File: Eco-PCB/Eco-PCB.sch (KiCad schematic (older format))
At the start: 14 parts, among them J1 DB25_Female, M1 SD Card, M1_1 XSOURCE Wireless, P1 Power_Block

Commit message: Removed unnecessary files and only kept the updated ones
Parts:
- Arduino2, Arduino3, Master1: footprint Module:Arduino_Nano_WithMountingHoles -> Module:Arduino_Nano; symbol arduino_nano:Arduino_Nano -> Eco-PCB-rescue:Arduino_Nano-arduino_nano
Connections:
- net labels added: RX_, SET, TX_
- wire segments 178 -> 202
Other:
- note added: "DT and SW for encoder from \nD14 & D15 to DSUB pins 8 & 7 respectively"

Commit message: Pcb 1 design done V1.0
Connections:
- net GND: now also J1.25 (P25); no longer J1.12
- net VCC: now also J1.13; no longer J1.25 (P25)
- net VCC_1: now also J1.23 (P23); no longer J1.13
- net at Master1.19 (AD0/D14): now also Arduino3.2 (D0/TX); no longer Arduino3.1 (D1/RX)
- net at Master1.20 (AD1/D15): now also Arduino3.1 (D1/RX); no longer Arduino3.2 (D0/TX)
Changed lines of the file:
@@
 	6050 1700 5800 1700
-Wire Wire Line
-	6350 3800 6350 3200
-Wire Wire Line
-	6350 3200 5800 3200
-Wire Wire Line
-	6450 3700 6450 3100
-Wire Wire Line
-	6450 3100 5800 3100
 Wire Wire Line
 	3900 4400 3900 3650
@@
 	6450 3700 7100 3700
 Wire Wire Line
-	8450 1750 10700 1750
-Connection ~ 10700 1750
-Wire Wire Line
 	10700 1750 10700 3400
 Wire Wire Line
@@
 NoConn ~ 9250 4550
 Wire Wire Line
-	10700 1000 10700 1750
-Wire Wire Line
 	8450 3400 8800 3400
 Wire Wire Line
@@
 	8800 2750 10800 2750
 Wire Wire Line
-	10800 2750 10800 1000
-Wire Wire Line
 	10800 4950 10800 4600
 Wire Wire Line
 	7450 4950 10800 4950
-Connection ~ 10800 2750
 Wire Wire Line
 	5150 5800 10800 5800
@@
 	10800 5900 10900 5900
 Wire Wire Line
-	10900 5900 10900 1000
+	10900 5900 10900 1200
 Text Label 10700 6200 0    50   ~ 0
 GND
@@
 Wire Wire Line
 	5150 6550 5850 6550
+Connection ~ 10800 2750
+Wire Wire Line
+	10800 2750 10800 1100
+Wire Wire Line
+	10800 1100 10900 1100
+Wire Wire Line
+	10900 1100 10900 1000
+Wire Wire Line
+	10400 1200 10400 1000
+Wire Wire Line
+	10400 1200 10900 1200
+Wire Wire Line
+	10800 1000 10750 1000
+Wire Wire Line
+	10750 1000 10750 1750
+Connection ~ 10700 1750
+Wire Wire Line
+	10700 1750 10750 1750
+Wire Wire Line
+	8450 1750 10700 1750
+Wire Wire Line
+	6350 3100 5800 3100
+Wire Wire Line
+	6350 3100 6350 3800
+Wire Wire Line
+	6450 3050 5900 3050
+Wire Wire Line
+	5900 3050 5900 3200
+Wire Wire Line
+	5900 3200 5800 3200
+Wire Wire Line
+	6450 3050 6450 3700
 $EndSCHEMATC

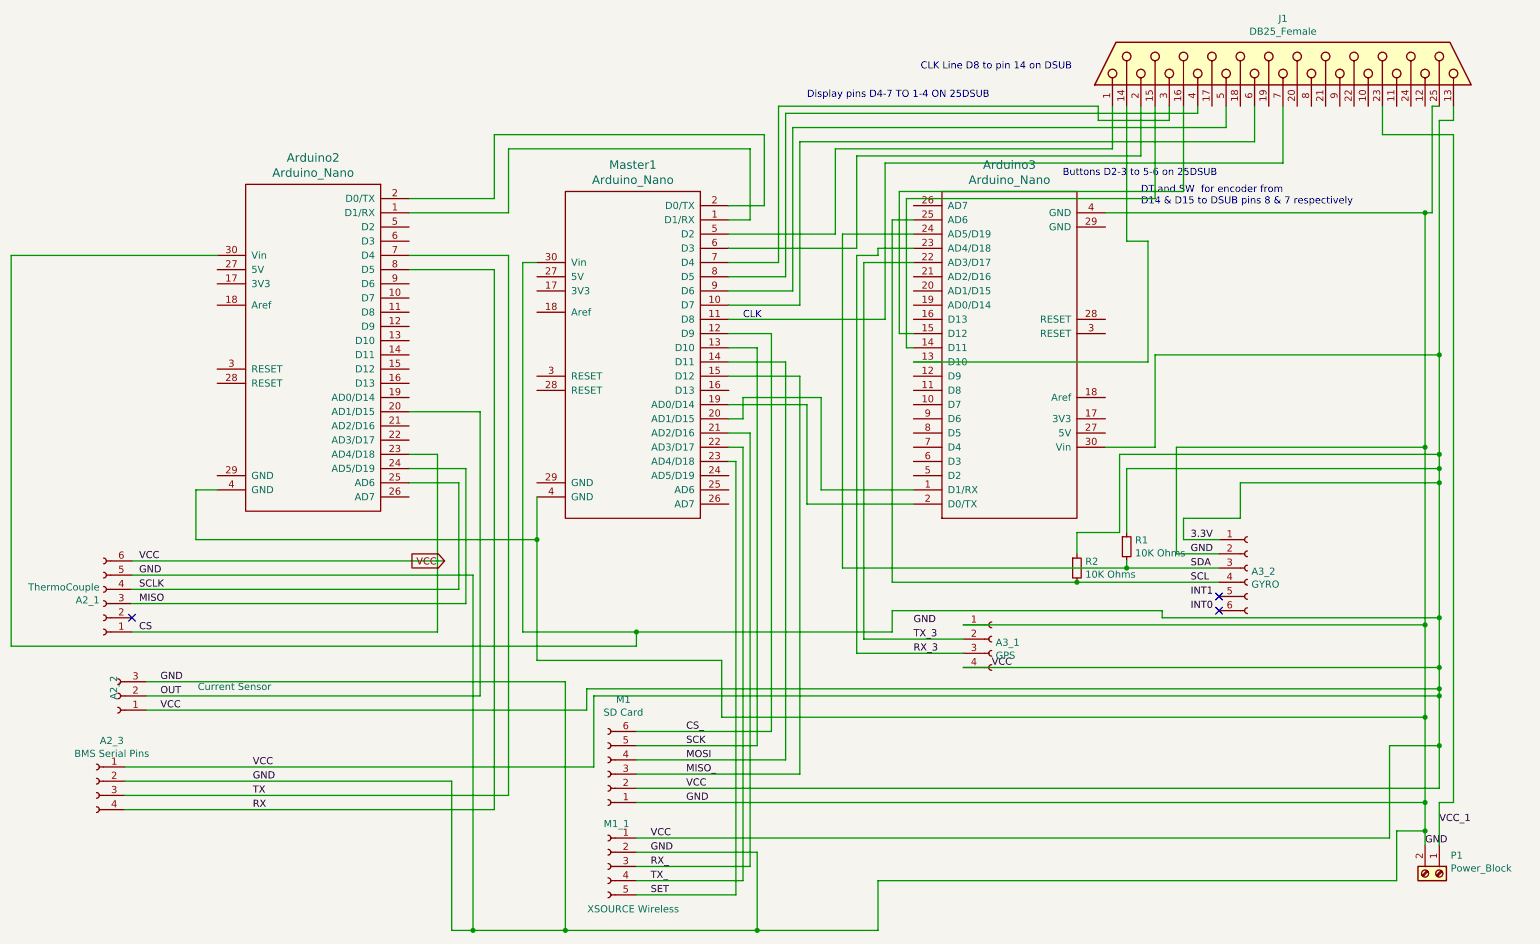
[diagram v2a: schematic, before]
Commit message: PCB1 added CLK line & PCB2 Design done
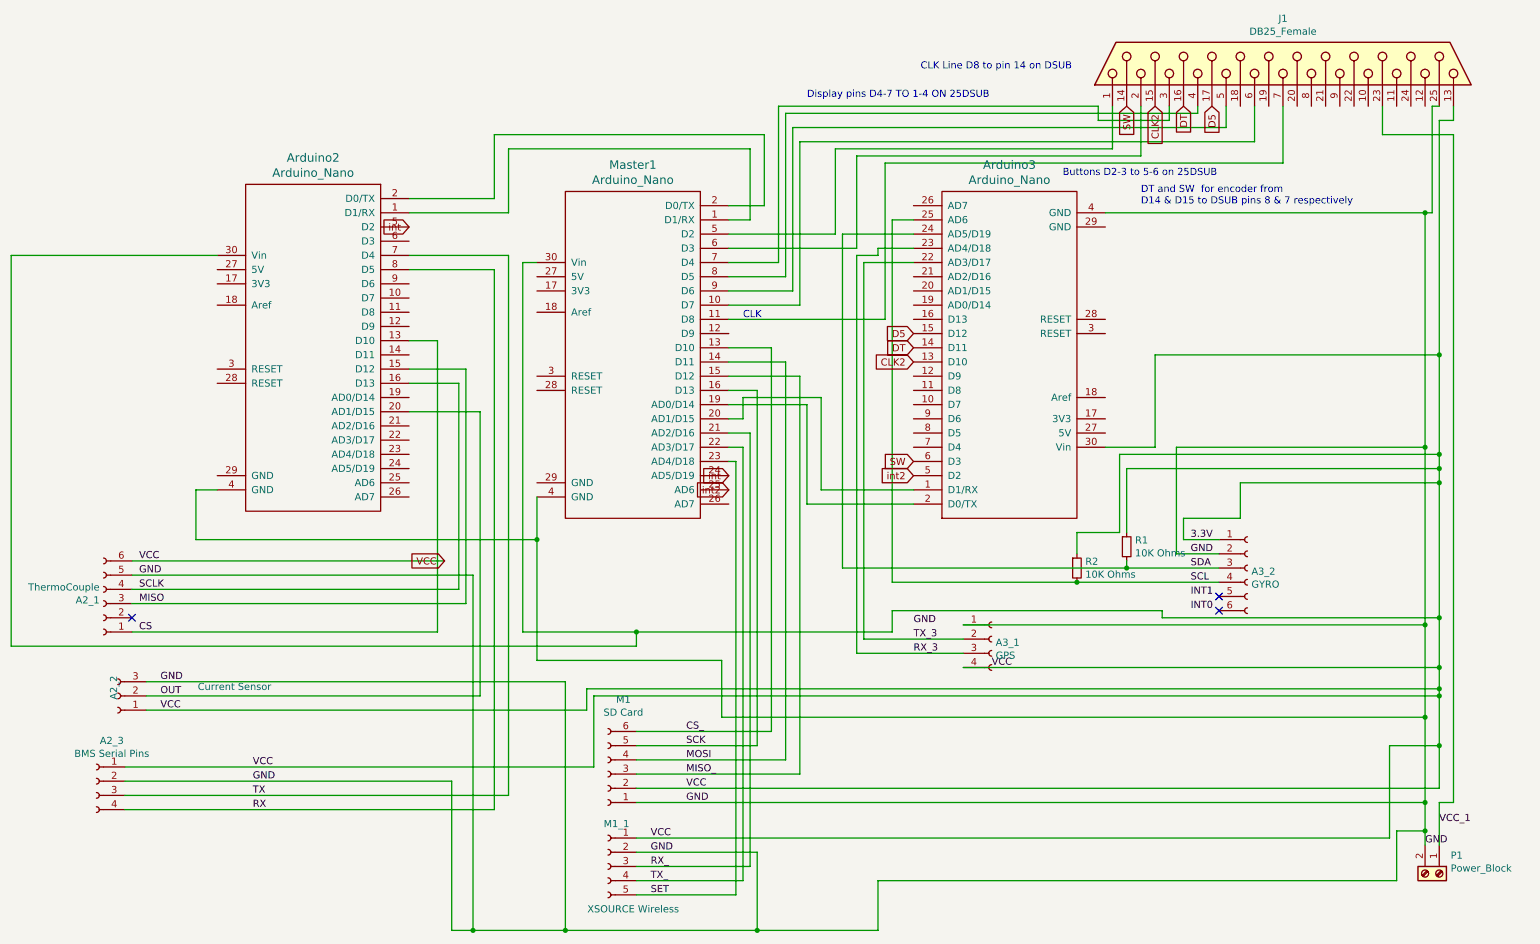
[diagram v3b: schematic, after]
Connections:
- net CS: now also Arduino2.13 (D10); no longer Arduino2.23 (AD4/D18)
- net CS_: now also Master1.13 (D10); no longer Master1.12 (D9)
- net MISO: now also Arduino2.15 (D12); no longer Arduino2.24 (AD5/D19)
- net SCK: now also Master1.16 (D13); no longer Master1.13 (D10)
- net SCLK: now also Arduino2.16 (D13); no longer Arduino2.25 (AD6)
- net int: now reaches Arduino2.5 (D2)
- net int: now also Master1.24 (AD5/D19)
- net int2: now reaches Master1.25 (AD6)
- net int2: now also Arduino3.5 (D2)
- net CLK2: now reaches Arduino3.13 (D10)
- net CLK2: now also J1.15 (P15); no longer J1.14 (P14)
- net DT: now reaches Arduino3.14 (D11)
- net DT: now also J1.16 (P16); no longer J1.15 (P15)
- net D5: now reaches Arduino3.15 (D12)
- net D5: now also J1.17 (P17); no longer J1.16 (P16)
- net SW: now reaches Arduino3.6 (D3)
- net SW: now also J1.14 (P14)

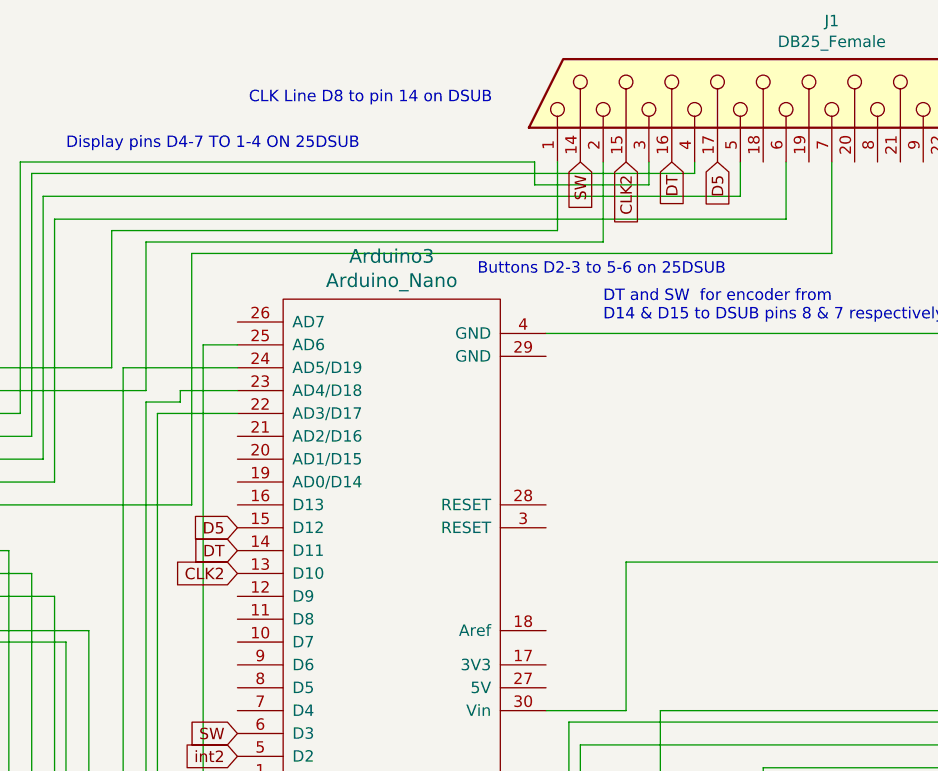
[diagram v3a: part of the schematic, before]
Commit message: updated pin sizes issue and spacing on PCB2
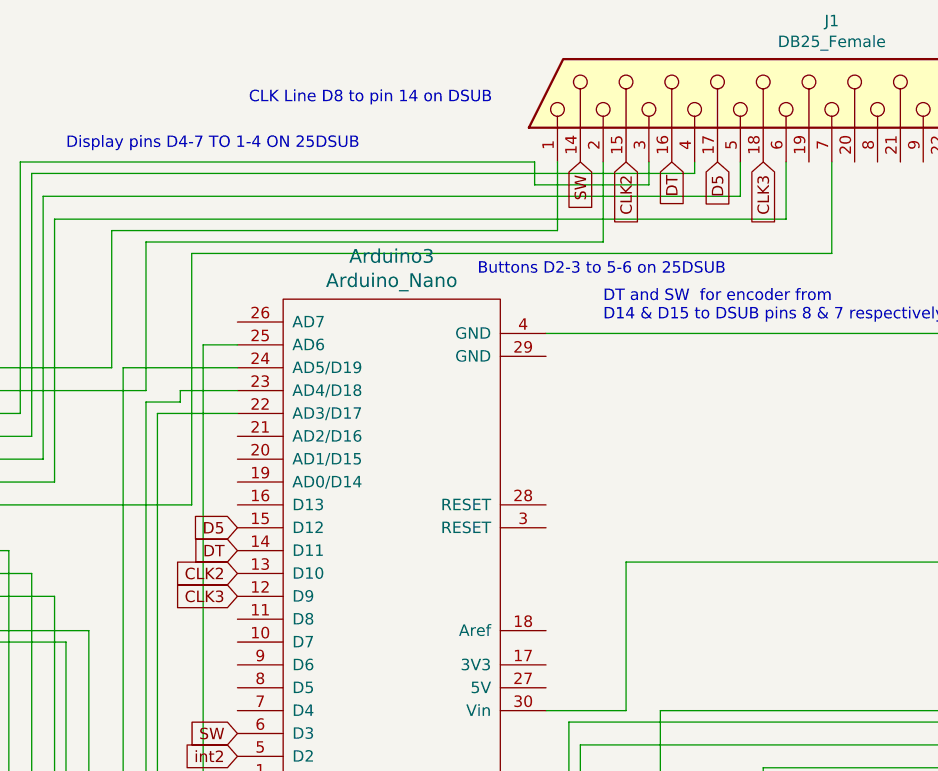
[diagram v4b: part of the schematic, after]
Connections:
- net CLK3: now reaches Arduino3.12 (D9)
- net CLK3: now also J1.18 (P18)
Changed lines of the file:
@@
 Text GLabel 9200 1000 3    50   Input ~ 0
 D5
+Text GLabel 7100 2900 0    50   Input ~ 0
+CLK3
+Text GLabel 9400 1000 3    50   Input ~ 0
+CLK3
 $EndSCHEMATC
